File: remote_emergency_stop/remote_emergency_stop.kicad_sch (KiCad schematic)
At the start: 1 part, among them U1 XIAO-ESP32S3

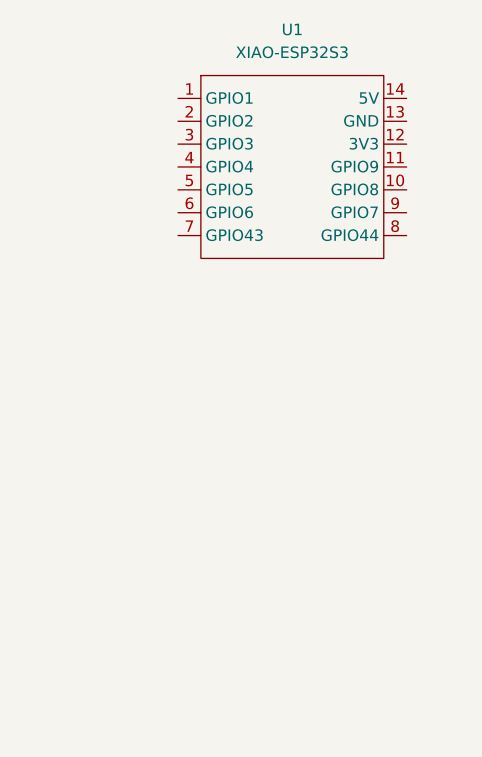
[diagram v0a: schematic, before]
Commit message: 通信モジュール決定
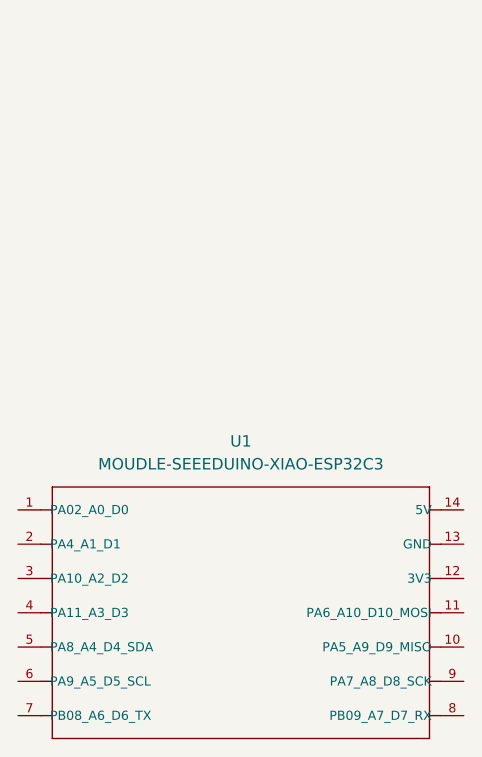
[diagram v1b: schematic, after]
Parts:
- removed U1: XIAO-ESP32S3, symbol GN10:XIAO-ESP32S3
- added U1: MOUDLE-SEEEDUINO-XIAO-ESP32C3, RF_Module:MCU_Seeed_ESP32C3, symbol MOUDLE-SEEEDUINO-XIAO-ESP32C3:MOUDLE-SEEEDUINO-XIAO-ESP32C3
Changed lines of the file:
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@@
 	(paper "A4")
 	(symbol
-		(lib_id "GN10:XIAO-ESP32S3")
-		(at 100.33 90.17 0)
+		(lib_id "MOUDLE-SEEEDUINO-XIAO-ESP32C3:MOUDLE-SEEEDUINO-XIAO-ESP32C3")
+		(at 95.25 139.7 0)
 		(unit 1)
 		(exclude_from_sim no)
@@
 		(fields_autoplaced yes)
 		(property "Reference" "U1"
-			(at 100.33 74.93 0)
+			(at 94.615 120.65 0)
 			(effects
 				(font
@@
 			)
 		)
-		(property "Value" "XIAO-ESP32S3"
-			(at 100.33 77.47 0)
+		(property "Value" "MOUDLE-SEEEDUINO-XIAO-ESP32C3"
+			(at 94.615 123.19 0)
 			(effects
 				(font
@@
 			)
 		)
-		(property "Footprint" ""
-			(at 100.33 90.17 0)
+		(property "Footprint" "RF_Module:MCU_Seeed_ESP32C3"
+			(at 95.25 139.7 0)
 			(effects
 				(font
 					(size 1.27 1.27)
 				)
+				(justify bottom)
 				(hide yes)
 			)
 		)
-		(property "Datasheet" "https://files.seeedstudio.com/wiki/SeeedStudio-XIAO-ESP32S3/res/esp32-s3_datasheet.pdf"
-			(at 100.33 90.17 0)
+		(property "Datasheet" ""
+			(at 95.25 139.7 0)
 			(effects
 				(font
@@
 		)
 		(property "Description" ""
-			(at 100.33 90.17 0)
+			(at 95.25 139.7 0)
 			(effects
 				(font
@@
 			)
 		)
-		(pin "7"
+		(pin "4"
 		)
 		(pin "9"
 		)
-		(pin "13"
+		(pin "7"
+		)
+		(pin "10"
+		)
+		(pin "8"
 		)
 		(pin "6"
 		)
-		(pin "8"
+		(pin "1"
 		)
 		(pin "12"
 		)
-		(pin "14"
-		)
-		(pin "1"
-		)
 		(pin "3"
-		)
-		(pin "11"
 		)
 		(pin "2"
@@
 		(pin "5"
 		)
-		(pin "10"
+		(pin "14"
 		)
-		(pin "4"
+		(pin "11"
+		)
+		(pin "13"
 		)
 		(instances

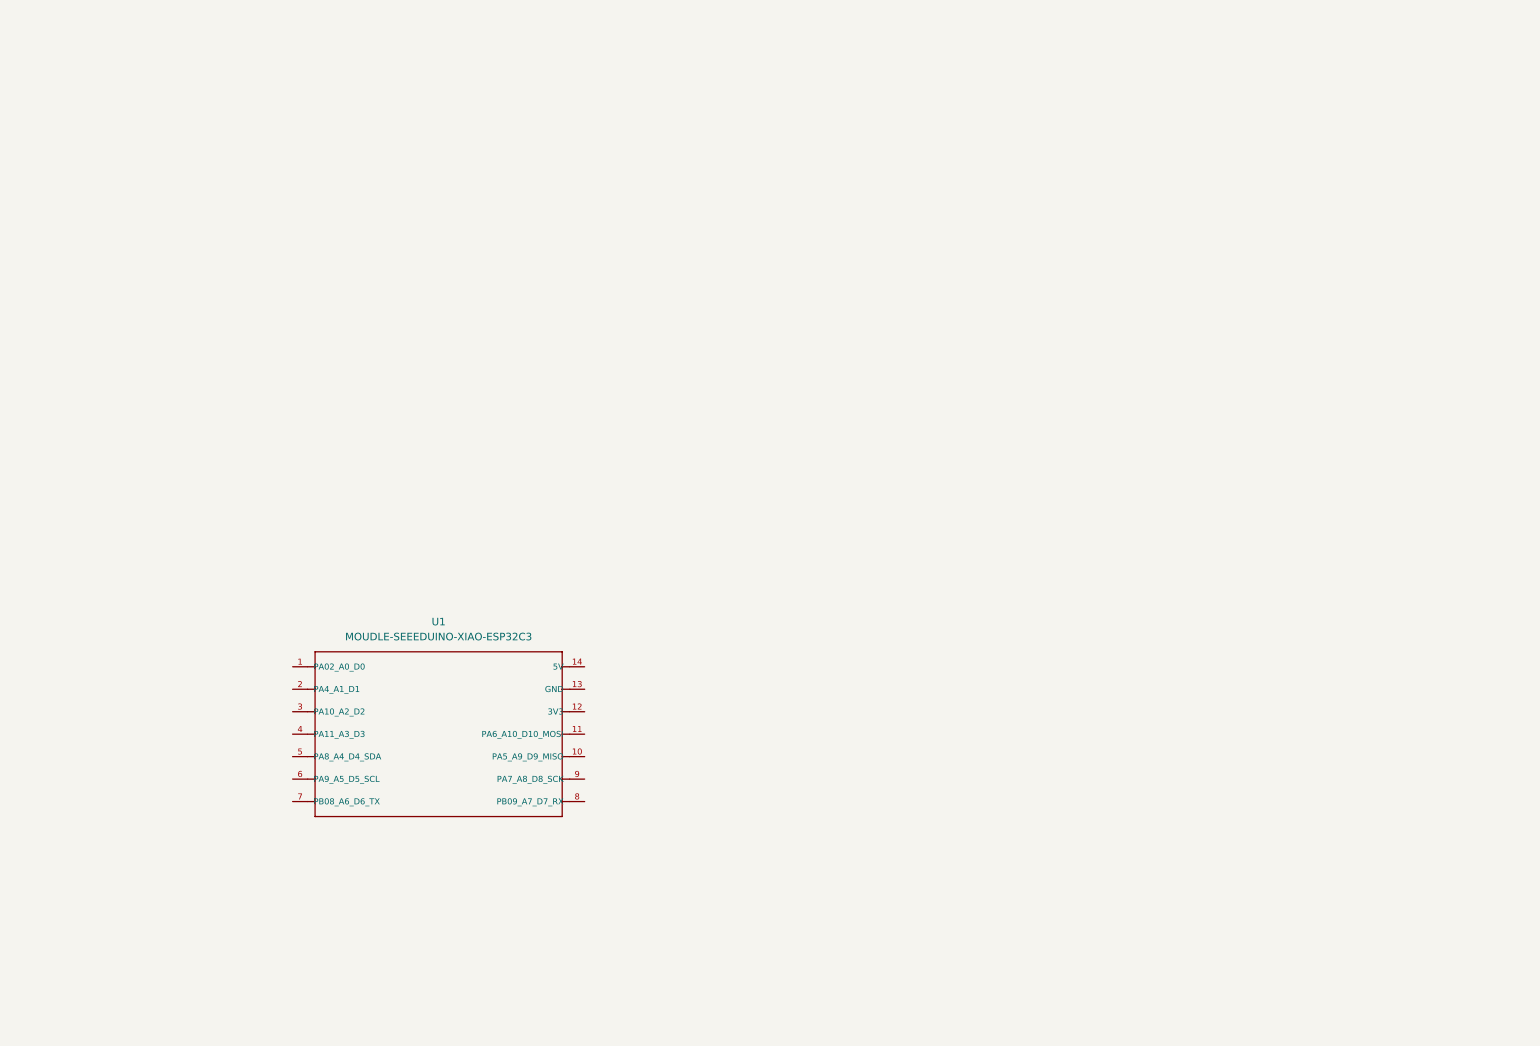
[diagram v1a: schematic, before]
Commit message: ESP32とIOをすこしまとめた
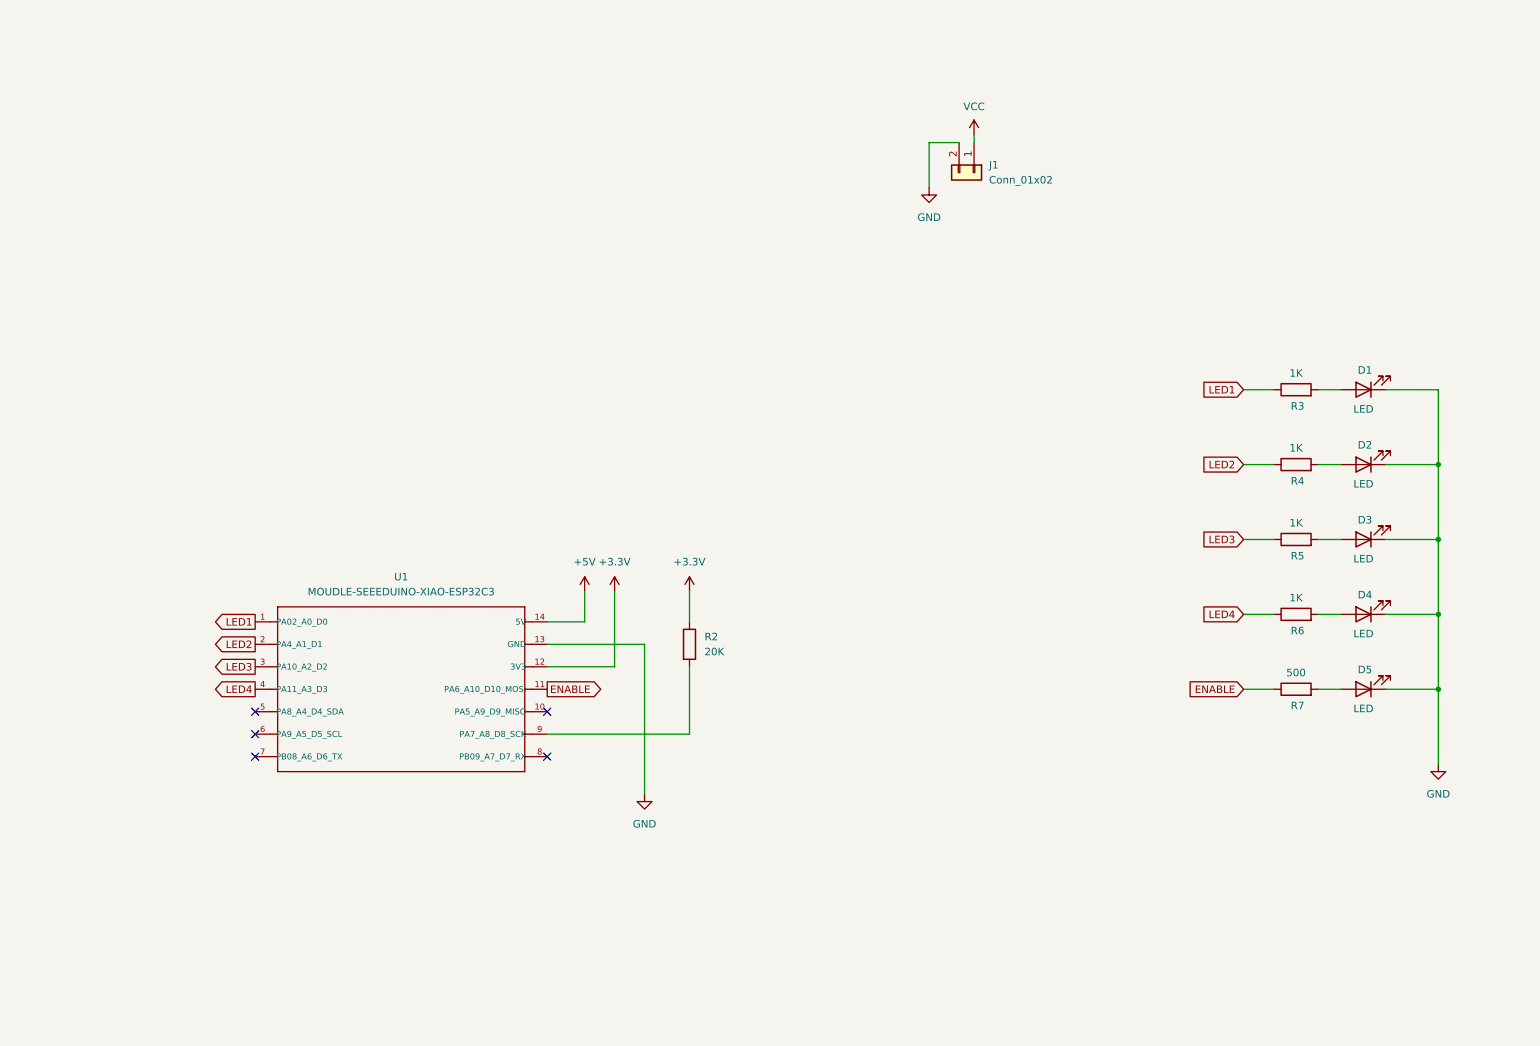
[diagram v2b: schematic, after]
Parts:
- added D1, D2, D3, D4, D5: LED, symbol Device:LED
- added J1: Conn_01x02, Connector_AMASS:AMASS_XT30U-M_1x02_P5.0mm_Vertical, symbol Connector_Generic:Conn_01x02
- added R2: 20K, symbol Device:R
- added R3, R4, R5, R6: 1K, symbol Device:R
- added R7: 500, symbol Device:R
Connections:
- net LED1: now reaches U1.1 (PA02_A0_D0)
- net LED1: now also R3.1
- net ENABLE: now reaches U1.11 (PA6_A10_D10_MOSI)
- net ENABLE: now also R7.1
- net +3.3V: now reaches U1.12 (3V3)
- net +3.3V: now also R2.1
- net GND: now reaches U1.13 (GND)
- net GND: now also D1.1 (K), D2.1 (K), D3.1 (K), D4.1 (K), D5.1 (K), J1.2 (Pin_2)
- net +5V: now reaches U1.14 (5V)
- net LED2: now reaches U1.2 (PA4_A1_D1)
- net LED2: now also R4.1
- net LED3: now reaches U1.3 (PA10_A2_D2)
- net LED3: now also R5.1
- net LED4: now reaches U1.4 (PA11_A3_D3)
- net LED4: now also R6.1
- net at U1.9 (PA7_A8_D8_SCK): now also R2.2
- new net: D4.2 (A), R6.2
- new net: D5.2 (A), R7.2
- new net: D1.2 (A), R3.2
- new net: D2.2 (A), R4.2
- new net: D3.2 (A), R5.2
- new net VCC: J1.1 (Pin_1)
- no-connect marks 0 -> 5
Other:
- moved on the sheet: U1

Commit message: こりゃだめだ、ユーザーインタフェイスが整ってない。
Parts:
- removed R2: 20K, symbol Device:R
- D1, D2, D3, D4, D5: footprint (none) -> LED_SMD:LED_0603_1608Metric_Pad1.05x0.95mm_HandSolder
- J1: footprint Connector_AMASS:AMASS_XT30U-M_1x02_P5.0mm_Vertical -> Connector_JST:JST_XH_S2B-XH-A_1x02_P2.50mm_Horizontal
- R3, R4, R5, R6, R7: footprint (none) -> Resistor_SMD:R_0603_1608Metric_Pad0.98x0.95mm_HandSolder
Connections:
- net VCC is gone; now on net GND: J1.1 (Pin_1)
- net GND: no longer J1.2 (Pin_2)
- net SW: now reaches U1.5 (PA8_A4_D4_SDA)
- new net 5V: J1.2 (Pin_2)
- no-connect marks 5 -> 3
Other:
- moved on the sheet: D1, D2, D3, D4, D5, J1, R3, R4, R5, R6, R7

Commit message: 遠隔非常停止は回路だけ完成した気がする
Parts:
- removed D2, D5: LED, LED_SMD:LED_0603_1608Metric_Pad1.05x0.95mm_HandSolder, symbol Device:LED
- added BZ1: Buzzer, Buzzer_Beeper:Buzzer_12x9.5RM7.6, symbol Device:Buzzer
- added J2: Conn_01x02, Connector_JST:JST_XH_S2B-XH-A_1x02_P2.50mm_Horizontal, symbol Connector_Generic:Conn_01x02
- added Q1: BSS138, Package_TO_SOT_SMD:SOT-23, symbol Transistor_FET:AO3400A
- added R1, R2: 220K, Resistor_SMD:R_0603_1608Metric, symbol Device:R
- added R10, R6: 1K, Resistor_SMD:R_0603_1608Metric, symbol Device:R
- added R8: 500, Resistor_SMD:R_0603_1608Metric, symbol Device:R
- added SW1: SW_DIP_x02, Button_Switch_SMD:SW_DIP_SPSTx02_Slide_Omron_A6H-2101_W6.15mm_P1.27mm, symbol Switch:SW_DIP_x02
- D1: value LED -> Yellow
- D2: renamed from D4; value LED -> Blue
- D3: value LED -> Red
- R3, R4, R5: value 1K -> 10K; footprint Resistor_SMD:R_0603_1608Metric_Pad0.98x0.95mm_HandSolder -> Resistor_SMD:R_0603_1608Metric
- R7: value 500 -> 20K; footprint Resistor_SMD:R_0603_1608Metric_Pad0.98x0.95mm_HandSolder -> Resistor_SMD:R_0603_1608Metric
- R9: renamed from R6; footprint Resistor_SMD:R_0603_1608Metric_Pad0.98x0.95mm_HandSolder -> Resistor_SMD:R_0603_1608Metric
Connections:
- net +3.3V: now also BZ1.1 (+), J2.1 (Pin_1), R8.1, SW1.1, SW1.2
- net 5V: now also R1.1
- net ENABLE: now also U1.3 (PA10_A2_D2), R6.1; no longer R7.1, U1.11 (PA6_A10_D10_MOSI)
- net GND: now also R3.2, R4.2, R5.1, R7.2, Q1.2 (S), R2.2; no longer D1.1 (K)
- net SW: now also R5.2, U1.6 (PA9_A5_D5_SCL), J2.2 (Pin_2); no longer U1.5 (PA8_A4_D4_SDA)
- net at D1.2 (A): now also R8.2; no longer R3.2
- net at D3.2 (A): now also R10.2; no longer R5.2
- net BAT_LOW: now reaches U1.8 (PB09_A7_D7_RX)
- net BAT_LOW: now also R10.1
- net LED1 renamed BAT_LEVEL
- net BAT_LEVEL: now also R1.2, R2.1; no longer R3.1
- net LED2 renamed DIP2
- net DIP2: now also U1.5 (PA8_A4_D4_SDA), SW1.3; no longer U1.2 (PA4_A1_D1)
- removed net LED3: R5.1, U1.3 (PA10_A2_D2)
- net LED4 renamed DIP1
- net DIP1: now also R3.1, SW1.4; no longer R9.1
- new net: BZ1.2 (-), D1.1 (K), Q1.3 (D)
- new net: Q1.1 (G), R6.2, R7.1
- new net WIRELESS: R9.1, U1.2 (PA4_A1_D1)
- no-connect marks 3 -> 4
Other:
- moved on the sheet: D2, J1, R9, U1

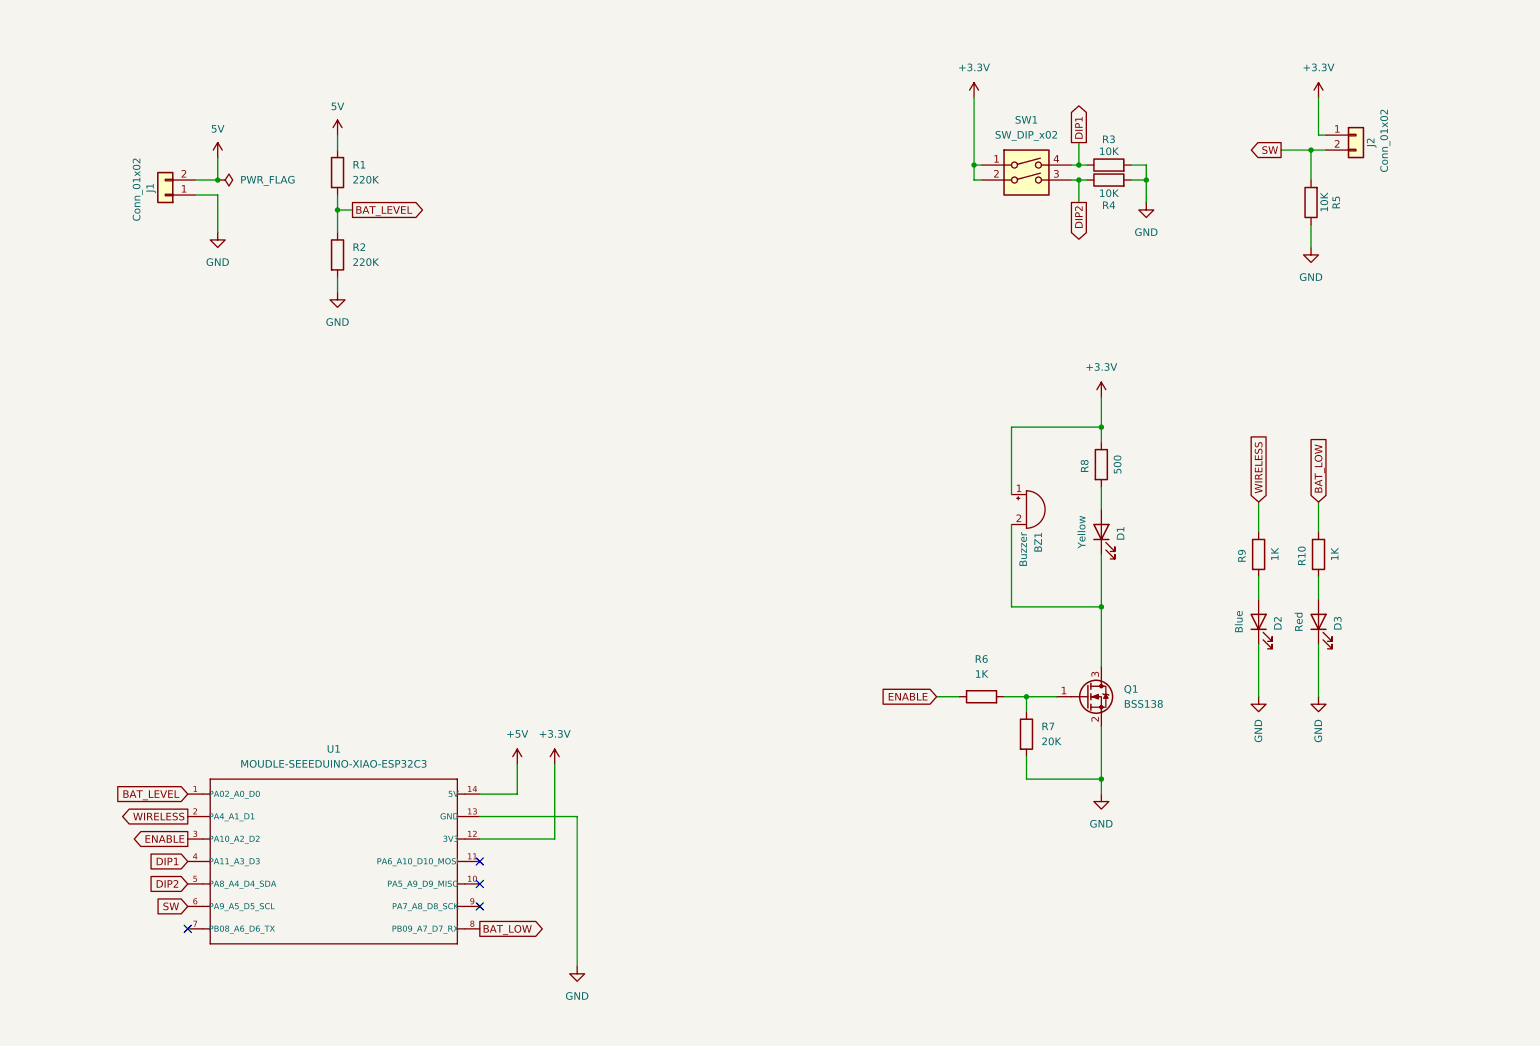
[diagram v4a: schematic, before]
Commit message: 遠隔非常停止のフットプリント決定した。回路にコンデンサ追加
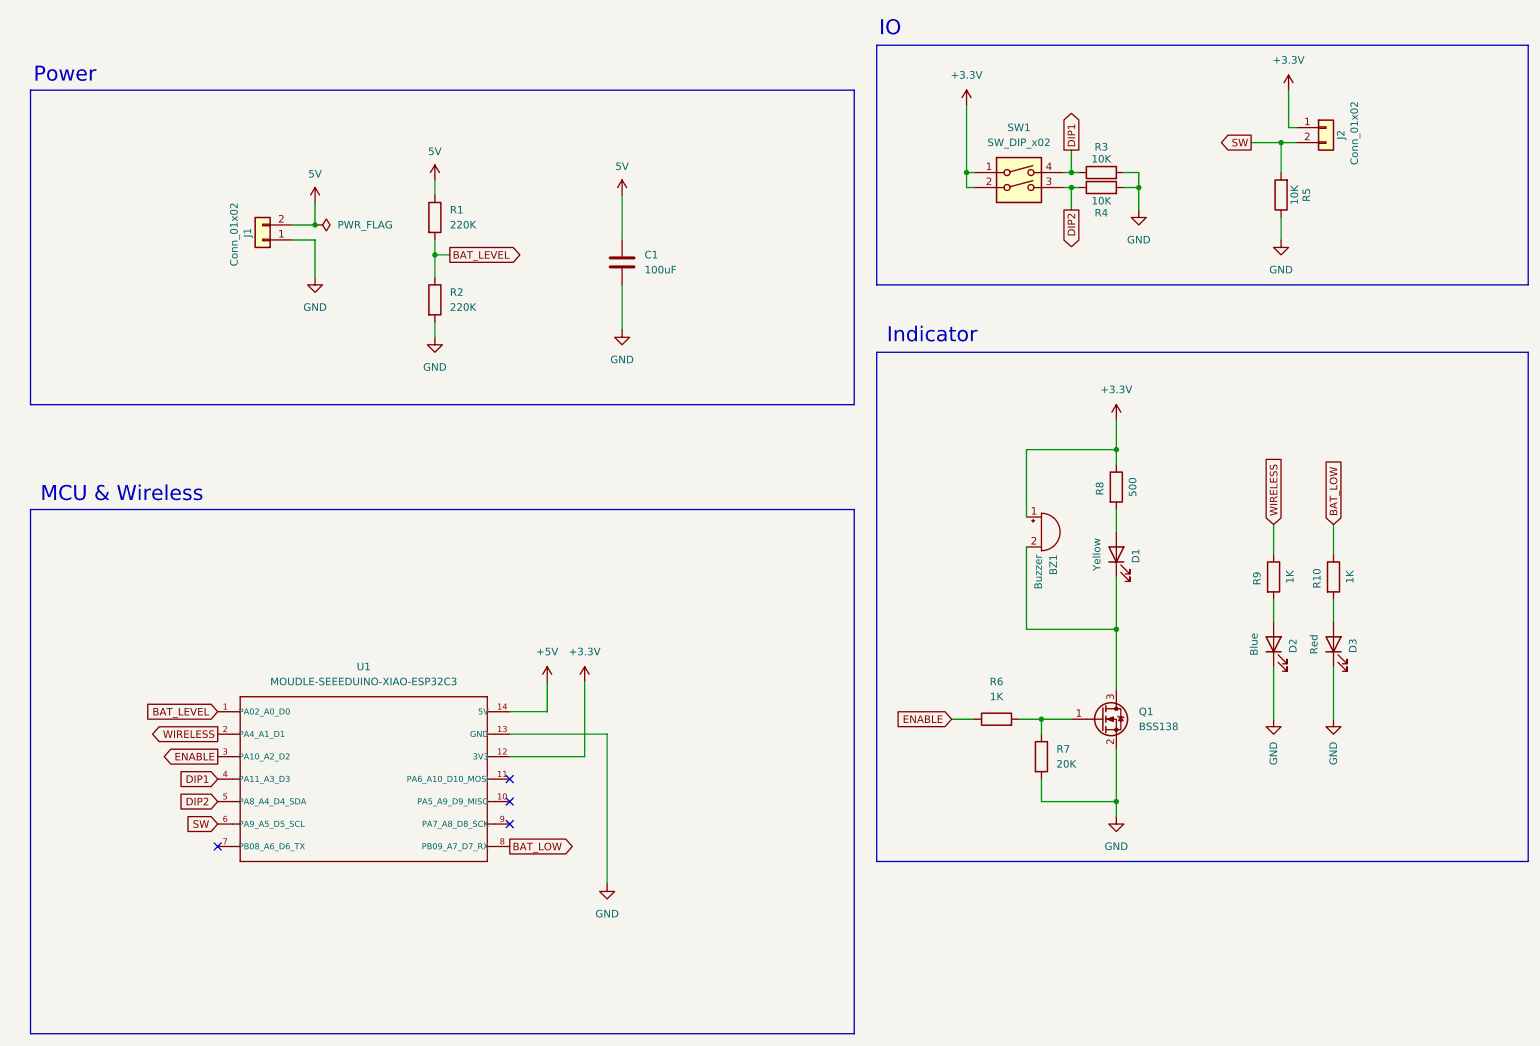
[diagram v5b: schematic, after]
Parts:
- added C1: 100uF, Capacitor_THT:CP_Radial_D5.0mm_P2.00mm, symbol Device:C
- J1: footprint Connector_JST:JST_XH_S2B-XH-A_1x02_P2.50mm_Horizontal -> Connector_AMASS:AMASS_XT30PW-M_1x02_P2.50mm_Horizontal
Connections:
- net 5V: now also C1.1
- net GND: now also C1.2
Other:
- note added: "IO"
- note added: "Indicator"
- note added: "MCU & Wireless"
- note added: "Power"
- moved on the sheet: BZ1, D1, D2, D3, J1, J2, Q1, R1, R10, R2, R3, R4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

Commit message: 難しくてわかんないッピ
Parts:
- added J3: Conn_01x02, Connector_JST:JST_XH_S2B-XH-A_1x02_P2.50mm_Horizontal, symbol Connector_Generic:Conn_01x02
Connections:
- net ENABLE: now also J3.1 (Pin_1)
- net GND: now also J3.2 (Pin_2)
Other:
- moved on the sheet: J2, R3, R4, R5, SW1

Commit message: 尽きた
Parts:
- added R11: 1K, symbol Device:R
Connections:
- net ENABLE: now also R11.1; no longer J3.1 (Pin_1)
- new net: J3.1 (Pin_1), R11.2
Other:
- moved on the sheet: J2, J3, R3, R4, R5, SW1
